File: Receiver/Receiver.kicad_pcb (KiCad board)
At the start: 2 copper layers, 21.5 x 15.7 mm, 2 parts, among them J1 Conn_01x03, U1 TSSP4038

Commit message: gnd fills
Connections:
- net Net-(J1-Pin_3) renamed GND
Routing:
- added copper zone on B.Cu, net GND
- added copper zone on F.Cu, net GND
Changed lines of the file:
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@@
 	(net 0 "")
 	(net 1 "Net-(J1-Pin_2)")
-	(net 2 "Net-(J1-Pin_3)")
+	(net 2 "GND")
 	(net 3 "Net-(J1-Pin_1)")
 	(footprint "Connector_JST:JST_XH_S3B-XH-A-1_1x03_P2.50mm_Horizontal"
@@
 			(layers "*.Cu" "*.Mask")
 			(remove_unused_layers no)
-			(net 2 "Net-(J1-Pin_3)")
+			(net 2 "GND")
 			(pinfunction "Pin_3")
 			(pintype "passive")
@@
 			)
 		)
+		(property ki_fp_filters "TO_SP4038_VIS")
+		(sheetname "Root")
+		(sheetfile "Receiver.kicad_sch")
 		(attr through_hole)
 		(fp_line
@@
 			(layers "*.Cu" "*.Mask")
 			(remove_unused_layers no)
-			(net 2 "Net-(J1-Pin_3)")
+			(net 2 "GND")
 			(pinfunction "2")
 			(pintype "unspecified")
@@
 		(net 3)
 	)
+	(zone
+		(net 2)
+		(net_name "GND")
+		(layers "F&B.Cu")
+		(hatch edge 0.5)
+		(connect_pads
+			(clearance 0.5)
+		)
+		(min_thickness 0.25)
+		(filled_areas_thickness no)
+		(fill yes
+			(thermal_gap 0.5)
+			(thermal_bridge_width 0.5)
+		)
+		(polygon
+			(pts
+				(xy 185.8 75.2) (xy 212.6 74.2) (xy 212.4 97.4) (xy 185.4 96.6)
+			)
+		)
+	)
 )

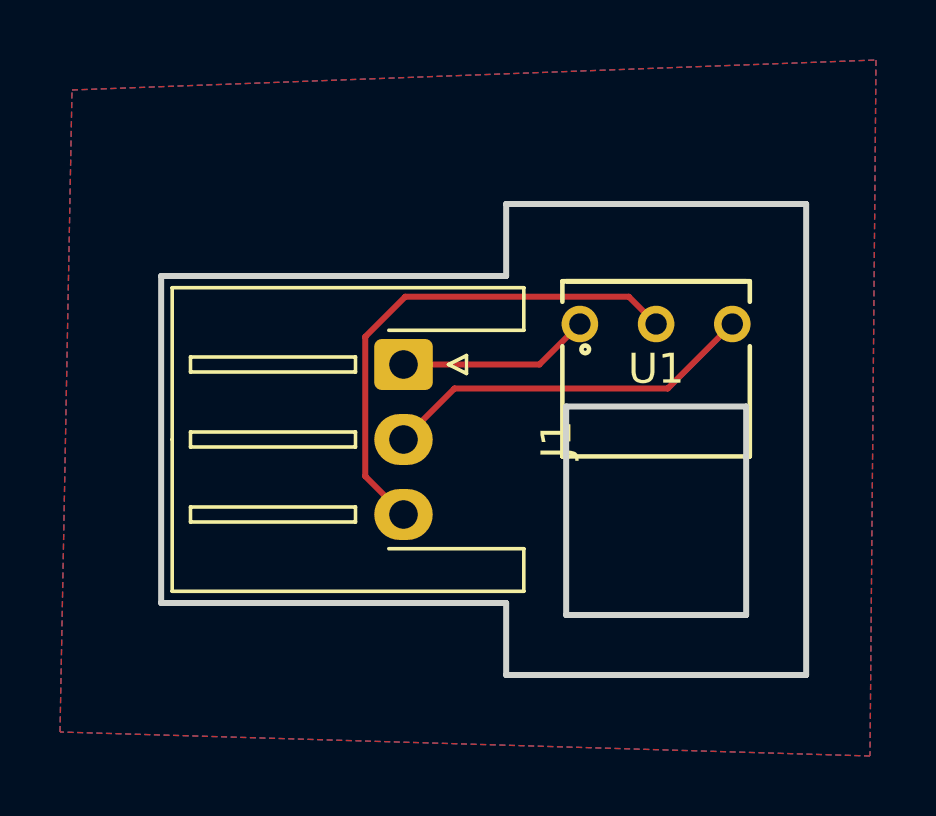
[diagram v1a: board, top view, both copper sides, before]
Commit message: Added low pass filter to reciever pcb
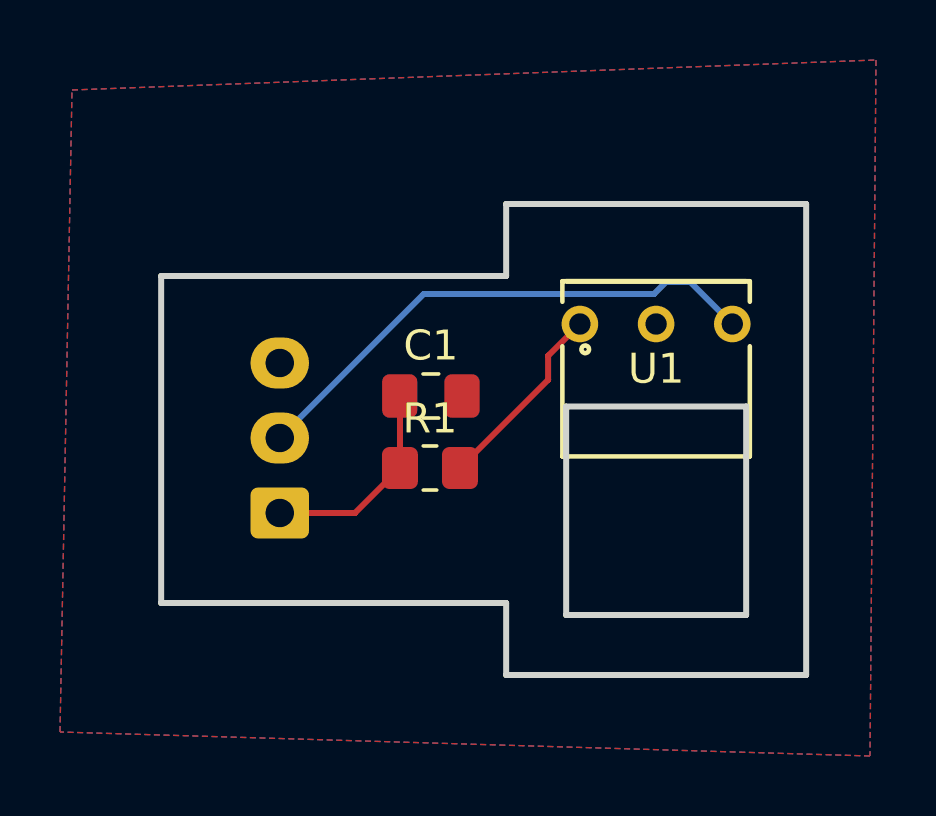
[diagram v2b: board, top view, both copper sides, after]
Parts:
- added C1: 0.1uF, Capacitor_SMD:C_0805_2012Metric_Pad1.18x1.45mm_HandSolder, F.Cu at (197.8, 85.4)
- added R1: 100k, Resistor_SMD:R_0805_2012Metric_Pad1.20x1.40mm_HandSolder, F.Cu at (197.7, 87.8)
- J1: footprint Connector_JST:JST_XH_S3B-XH-A-1_1x03_P2.50mm_Horizontal -> Connector_JST:JST_XH_B3B-XH-AM_1x03_P2.50mm_Vertical; moved to B.Cu
- moved J1 6.44 mm to (192.7, 89.3), turned to 90 degrees
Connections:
- U1 pad 1: Net-(J1-Pin_1) -> Net-(R1-Pad2)
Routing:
- net GND: track 17.1 -> 0.00 mm
- net Net-(R1-Pad2): track 0.00 -> 6.46 mm
- net Net-(J1-Pin_2): track 12.6 -> 17.8 mm
- net Net-(J1-Pin_1): track 6.44 -> 7.03 mm
